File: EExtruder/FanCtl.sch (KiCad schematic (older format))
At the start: 7 parts, among them J8 Conn_01x03_Male, Q5 SI2318CDS

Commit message: Component layout complete.
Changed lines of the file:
@@
 AR Path="/5BBB612D/5BBB5A51" Ref="Q6"  Part="1"
 AR Path="/5BBB62EB/5BBB5A51" Ref="Q7"  Part="1"
-F 0 "Q7" H 5905 3246 50  0000 L CNN
+F 0 "Q5" H 5905 3246 50  0000 L CNN
 F 1 "SI2318CDS" H 5905 3155 50  0000 L CNN
 F 2 "Package_TO_SOT_SMD:SOT-23" H 5900 3125 50  0001 L CIN
@@
 AR Path="/5BBB612D/5BBB5AB3" Ref="R25"  Part="1"
 AR Path="/5BBB62EB/5BBB5AB3" Ref="R28"  Part="1"
-F 0 "R28" V 5043 3200 50  0000 C CNN
+F 0 "R22" V 5043 3200 50  0000 C CNN
 F 1 "1k" V 5134 3200 50  0000 C CNN
 F 2 "Resistor_SMD:R_0603_1608Metric" V 5180 3200 50  0001 C CNN
@@
 AR Path="/5BBB612D/5BBB5B30" Ref="R24"  Part="1"
 AR Path="/5BBB62EB/5BBB5B30" Ref="R27"  Part="1"
-F 0 "R27" H 5020 3446 50  0000 L CNN
+F 0 "R21" H 5020 3446 50  0000 L CNN
 F 1 "10k" H 5020 3355 50  0000 L CNN
 F 2 "Resistor_SMD:R_0603_1608Metric" V 4880 3400 50  0001 C CNN
@@
 AR Path="/5BBB612D/5BBB5B8C" Ref="D9"  Part="1"
 AR Path="/5BBB62EB/5BBB5B8C" Ref="D11"  Part="1"
-F 0 "D11" V 5754 2879 50  0000 L CNN
+F 0 "D7" V 5754 2879 50  0000 L CNN
 F 1 "1N4148" V 5845 2879 50  0000 L CNN
 F 2 "Diode_SMD:D_SOD-323_HandSoldering" H 5800 2625 50  0001 C CNN
@@
 AR Path="/5BBB612D/5BBF7CFC" Ref="R26"  Part="1"
 AR Path="/5BBB62EB/5BBF7CFC" Ref="R29"  Part="1"
-F 0 "R29" V 7293 3000 50  0000 C CNN
+F 0 "R23" V 7293 3000 50  0000 C CNN
 F 1 "10k" V 7384 3000 50  0000 C CNN
 F 2 "Resistor_SMD:R_0603_1608Metric" V 7430 3000 50  0001 C CNN
@@
 AR Path="/5BBB612D/5BBF8D0E" Ref="D10"  Part="1"
 AR Path="/5BBB62EB/5BBF8D0E" Ref="D12"  Part="1"
-F 0 "D12" H 7850 3216 50  0000 C CNN
+F 0 "D8" H 7850 3216 50  0000 C CNN
 F 1 "1N4148" H 7850 3125 50  0000 C CNN
 F 2 "Diode_SMD:D_SOD-323_HandSoldering" H 7850 3000 50  0001 C CNN
@@
 AR Path="/5BBB56F0/5BDBC1F3" Ref="J7"  Part="1"
 AR Path="/5BBB62EB/5BDBC1F3" Ref="J9"  Part="1"
-F 0 "J9" H 6722 3482 50  0000 R CNN
+F 0 "J7" H 6722 3482 50  0000 R CNN
 F 1 "Conn_01x03_Male" H 6722 3573 50  0000 R CNN
 F 2 "Connector_PinHeader_2.54mm:PinHeader_1x03_P2.54mm_Vertical" H 6750 3550 50  0001 C CNN

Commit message: Ready to manufacture.
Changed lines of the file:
@@
 AR Path="/5BBB612D/5BBB5A51" Ref="Q6"  Part="1"
 AR Path="/5BBB62EB/5BBB5A51" Ref="Q7"  Part="1"
-F 0 "Q5" H 5905 3246 50  0000 L CNN
+F 0 "Q7" H 5905 3246 50  0000 L CNN
 F 1 "SI2318CDS" H 5905 3155 50  0000 L CNN
 F 2 "Package_TO_SOT_SMD:SOT-23" H 5900 3125 50  0001 L CIN
@@
 AR Path="/5BBB612D/5BBB5AB3" Ref="R25"  Part="1"
 AR Path="/5BBB62EB/5BBB5AB3" Ref="R28"  Part="1"
-F 0 "R22" V 5043 3200 50  0000 C CNN
+F 0 "R28" V 5043 3200 50  0000 C CNN
 F 1 "1k" V 5134 3200 50  0000 C CNN
 F 2 "Resistor_SMD:R_0603_1608Metric" V 5180 3200 50  0001 C CNN
@@
 AR Path="/5BBB612D/5BBB5B30" Ref="R24"  Part="1"
 AR Path="/5BBB62EB/5BBB5B30" Ref="R27"  Part="1"
-F 0 "R21" H 5020 3446 50  0000 L CNN
+F 0 "R27" H 5020 3446 50  0000 L CNN
 F 1 "10k" H 5020 3355 50  0000 L CNN
 F 2 "Resistor_SMD:R_0603_1608Metric" V 4880 3400 50  0001 C CNN
@@
 AR Path="/5BBB612D/5BBB5B8C" Ref="D9"  Part="1"
 AR Path="/5BBB62EB/5BBB5B8C" Ref="D11"  Part="1"
-F 0 "D7" V 5754 2879 50  0000 L CNN
+F 0 "D11" V 5754 2879 50  0000 L CNN
 F 1 "1N4148" V 5845 2879 50  0000 L CNN
 F 2 "Diode_SMD:D_SOD-323_HandSoldering" H 5800 2625 50  0001 C CNN
@@
 AR Path="/5BBB612D/5BBF7CFC" Ref="R26"  Part="1"
 AR Path="/5BBB62EB/5BBF7CFC" Ref="R29"  Part="1"
-F 0 "R23" V 7293 3000 50  0000 C CNN
+F 0 "R29" V 7293 3000 50  0000 C CNN
 F 1 "10k" V 7384 3000 50  0000 C CNN
 F 2 "Resistor_SMD:R_0603_1608Metric" V 7430 3000 50  0001 C CNN
@@
 AR Path="/5BBB612D/5BBF8D0E" Ref="D10"  Part="1"
 AR Path="/5BBB62EB/5BBF8D0E" Ref="D12"  Part="1"
-F 0 "D8" H 7850 3216 50  0000 C CNN
+F 0 "D12" H 7850 3216 50  0000 C CNN
 F 1 "1N4148" H 7850 3125 50  0000 C CNN
 F 2 "Diode_SMD:D_SOD-323_HandSoldering" H 7850 3000 50  0001 C CNN
@@
 AR Path="/5BBB56F0/5BDBC1F3" Ref="J7"  Part="1"
 AR Path="/5BBB62EB/5BDBC1F3" Ref="J9"  Part="1"
-F 0 "J7" H 6722 3482 50  0000 R CNN
+F 0 "J9" H 6722 3482 50  0000 R CNN
 F 1 "Conn_01x03_Male" H 6722 3573 50  0000 R CNN
 F 2 "Connector_PinHeader_2.54mm:PinHeader_1x03_P2.54mm_Vertical" H 6750 3550 50  0001 C CNN

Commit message: Select correct terminals. Use old style square footprints.
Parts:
- R21, R22, R23: footprint Resistor_SMD:R_0603_1608Metric -> Local:R_0603_1608Metric
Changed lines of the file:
@@
 $Descr A4 11693 8268
 encoding utf-8
-Sheet 7 8
+Sheet 8 8
 Title ""
 Date ""
@@
 F 0 "R28" V 5043 3200 50  0000 C CNN
 F 1 "1k" V 5134 3200 50  0000 C CNN
-F 2 "Resistor_SMD:R_0603_1608Metric" V 5180 3200 50  0001 C CNN
+F 2 "Local:R_0603_1608Metric" V 5180 3200 50  0001 C CNN
 F 3 "~" H 5250 3200 50  0001 C CNN
 	1    5250 3200
@@
 F 0 "R27" H 5020 3446 50  0000 L CNN
 F 1 "10k" H 5020 3355 50  0000 L CNN
-F 2 "Resistor_SMD:R_0603_1608Metric" V 4880 3400 50  0001 C CNN
+F 2 "Local:R_0603_1608Metric" V 4880 3400 50  0001 C CNN
 F 3 "~" H 4950 3400 50  0001 C CNN
 	1    4950 3400
@@
 F 0 "R29" V 7293 3000 50  0000 C CNN
 F 1 "10k" V 7384 3000 50  0000 C CNN
-F 2 "Resistor_SMD:R_0603_1608Metric" V 7430 3000 50  0001 C CNN
+F 2 "Local:R_0603_1608Metric" V 7430 3000 50  0001 C CNN
 F 3 "~" H 7500 3000 50  0001 C CNN
 	1    7500 3000

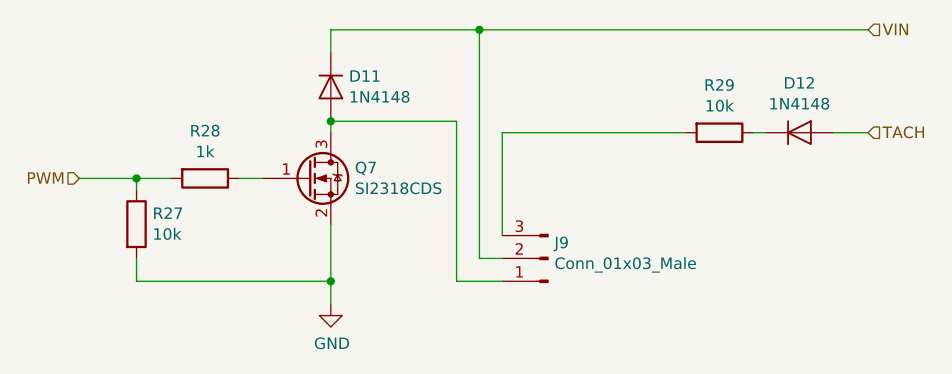
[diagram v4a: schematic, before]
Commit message: Added voltage selector for the fans.
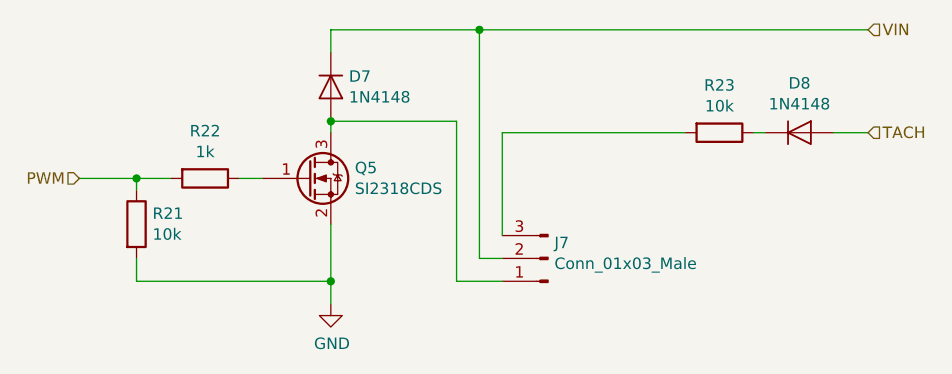
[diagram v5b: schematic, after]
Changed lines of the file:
@@
 $Descr A4 11693 8268
 encoding utf-8
-Sheet 8 8
+Sheet 6 8
 Title ""
 Date ""
@@
 AR Path="/5BBB612D/5BBB5A51" Ref="Q6"  Part="1"
 AR Path="/5BBB62EB/5BBB5A51" Ref="Q7"  Part="1"
-F 0 "Q7" H 5905 3246 50  0000 L CNN
+F 0 "Q5" H 5905 3246 50  0000 L CNN
 F 1 "SI2318CDS" H 5905 3155 50  0000 L CNN
 F 2 "Package_TO_SOT_SMD:SOT-23" H 5900 3125 50  0001 L CIN
@@
 AR Path="/5BBB612D/5BBB5AB3" Ref="R25"  Part="1"
 AR Path="/5BBB62EB/5BBB5AB3" Ref="R28"  Part="1"
-F 0 "R28" V 5043 3200 50  0000 C CNN
+F 0 "R22" V 5043 3200 50  0000 C CNN
 F 1 "1k" V 5134 3200 50  0000 C CNN
 F 2 "Local:R_0603_1608Metric" V 5180 3200 50  0001 C CNN
@@
 AR Path="/5BBB612D/5BBB5B30" Ref="R24"  Part="1"
 AR Path="/5BBB62EB/5BBB5B30" Ref="R27"  Part="1"
-F 0 "R27" H 5020 3446 50  0000 L CNN
+F 0 "R21" H 5020 3446 50  0000 L CNN
 F 1 "10k" H 5020 3355 50  0000 L CNN
 F 2 "Local:R_0603_1608Metric" V 4880 3400 50  0001 C CNN
@@
 AR Path="/5BBB612D/5BBB5B8C" Ref="D9"  Part="1"
 AR Path="/5BBB62EB/5BBB5B8C" Ref="D11"  Part="1"
-F 0 "D11" V 5754 2879 50  0000 L CNN
+F 0 "D7" V 5754 2879 50  0000 L CNN
 F 1 "1N4148" V 5845 2879 50  0000 L CNN
 F 2 "Diode_SMD:D_SOD-323_HandSoldering" H 5800 2625 50  0001 C CNN
@@
 AR Path="/5BBB612D/5BBB5C35" Ref="#PWR016"  Part="1"
 AR Path="/5BBB62EB/5BBB5C35" Ref="#PWR017"  Part="1"
-F 0 "#PWR017" H 5800 3500 50  0001 C CNN
+F 0 "#PWR015" H 5800 3500 50  0001 C CNN
 F 1 "GND" H 5805 3577 50  0000 C CNN
 F 2 "" H 5800 3750 50  0001 C CNN
@@
 AR Path="/5BBB612D/5BBF7CFC" Ref="R26"  Part="1"
 AR Path="/5BBB62EB/5BBF7CFC" Ref="R29"  Part="1"
-F 0 "R29" V 7293 3000 50  0000 C CNN
+F 0 "R23" V 7293 3000 50  0000 C CNN
 F 1 "10k" V 7384 3000 50  0000 C CNN
 F 2 "Local:R_0603_1608Metric" V 7430 3000 50  0001 C CNN
@@
 AR Path="/5BBB612D/5BBF8D0E" Ref="D10"  Part="1"
 AR Path="/5BBB62EB/5BBF8D0E" Ref="D12"  Part="1"
-F 0 "D12" H 7850 3216 50  0000 C CNN
+F 0 "D8" H 7850 3216 50  0000 C CNN
 F 1 "1N4148" H 7850 3125 50  0000 C CNN
 F 2 "Diode_SMD:D_SOD-323_HandSoldering" H 7850 3000 50  0001 C CNN
@@
 AR Path="/5BBB56F0/5BDBC1F3" Ref="J7"  Part="1"
 AR Path="/5BBB62EB/5BDBC1F3" Ref="J9"  Part="1"
-F 0 "J9" H 6722 3482 50  0000 R CNN
+F 0 "J7" H 6722 3482 50  0000 R CNN
 F 1 "Conn_01x03_Male" H 6722 3573 50  0000 R CNN
 F 2 "Connector_PinHeader_2.54mm:PinHeader_1x03_P2.54mm_Vertical" H 6750 3550 50  0001 C CNN
